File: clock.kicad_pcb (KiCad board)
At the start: 4 copper layers, 32 x 30 mm, 30 parts, among them J1 CONN_01X05, P1 USB_OTG, P2 CONN_01X02, U1 oled_i2c_display_128x64, U2 FM24V10-G, U3 STLCS01V1, U4 mcp73831, U5 lmv341, U6 NCP170

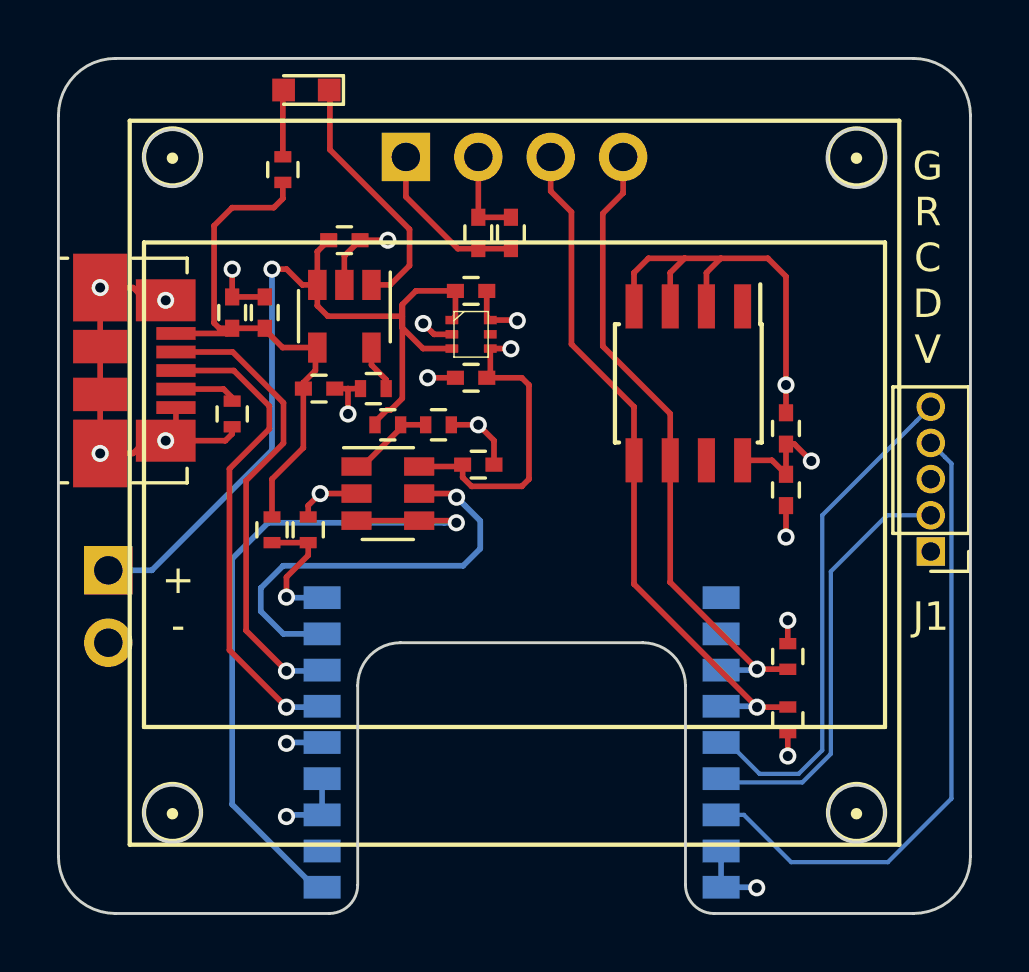
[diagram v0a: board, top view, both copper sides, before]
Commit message: modified ncp170 symbol because was totally wrong, F%*ç%
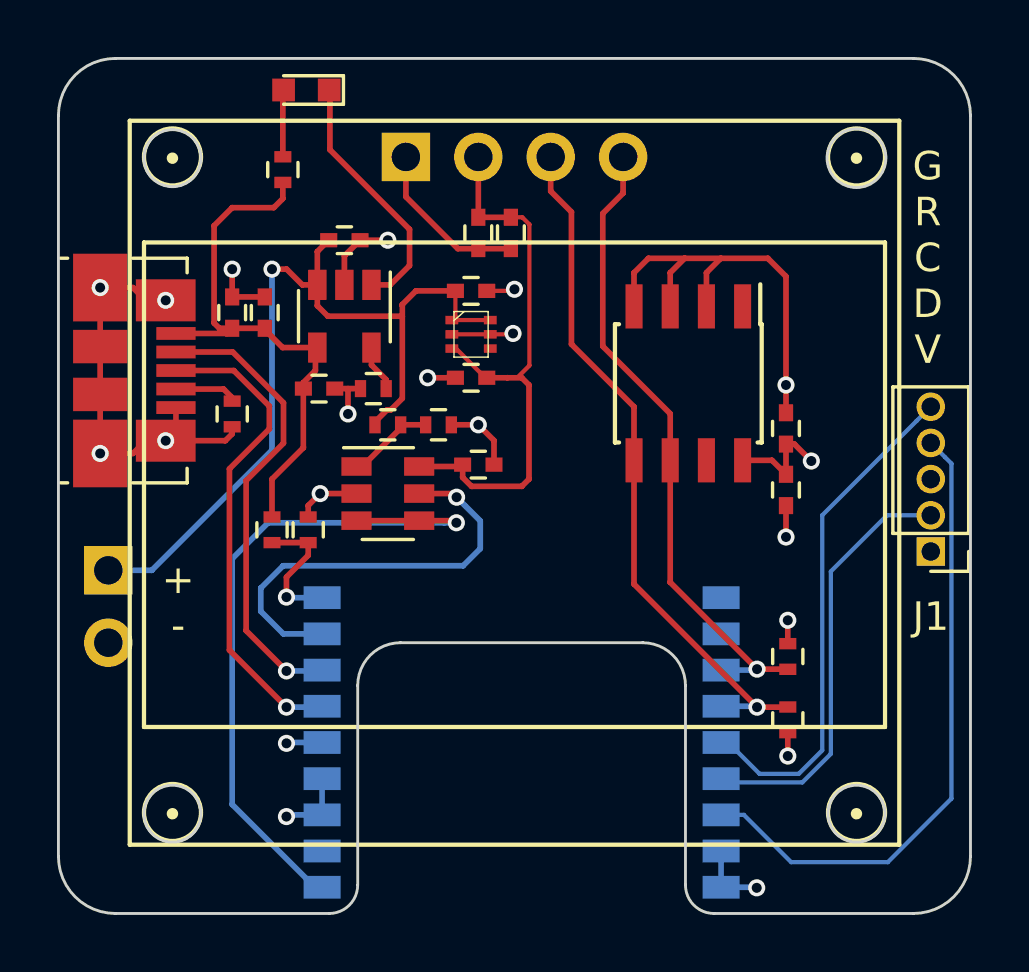
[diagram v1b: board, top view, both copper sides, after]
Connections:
- U6 pad 3: /VBAT -> VCC
- U6 pad 4: VCC -> (no net)
- U6 pad 5: (no net) -> GND
- U6 pad 6: GND -> /VBAT
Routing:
- net VCC: track 22.7 -> 29.4 mm, vias 5 -> 4
- net /VBAT: track 31.9 -> 30.5 mm
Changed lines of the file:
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@@
   (general
     (links 82)
-    (no_connects 0)
+    (no_connects 5)
     (area 149.949999 69.949999 182.050001 100.050001)
     (thickness 1.6)
     (drawings 30)
-    (tracks 264)
+    (tracks 265)
     (zones 0)
     (modules 30)
@@
       (net 1 GND))
     (pad 3 smd rect (at 0.5 0.675 270) (size 0.3 0.45) (layers F.Cu F.Paste F.Mask)
+      (net 2 VCC))
+    (pad 4 smd rect (at 0.5 -0.675 270) (size 0.3 0.45) (layers F.Cu F.Paste F.Mask))
+    (pad 5 smd rect (at 0 -0.675 270) (size 0.3 0.45) (layers F.Cu F.Paste F.Mask)
+      (net 1 GND))
+    (pad 6 smd rect (at -0.5 -0.675 270) (size 0.3 0.45) (layers F.Cu F.Paste F.Mask)
       (net 3 /VBAT))
-    (pad 4 smd rect (at 0.5 -0.675 270) (size 0.3 0.45) (layers F.Cu F.Paste F.Mask)
-      (net 2 VCC))
-    (pad 5 smd rect (at 0 -0.675 270) (size 0.3 0.45) (layers F.Cu F.Paste F.Mask))
-    (pad 6 smd rect (at -0.5 -0.675 270) (size 0.3 0.45) (layers F.Cu F.Paste F.Mask)
-      (net 1 GND))
   )
   (module Capacitors_SMD:C_0402 (layer F.Cu)
@@
   (gr_line (start 152 70) (end 180 70) (layer Edge.Cuts) (width 0.1))
   (gr_line (start 150 98) (end 150 72) (layer Edge.Cuts) (width 0.1))
+  (segment (start 165.92 79.68) (end 165.95 79.65) (width 0.15) (layer F.Cu) (net 1))
+  (segment (start 165.153 79.68) (end 165.92 79.68) (width 0.15) (layer F.Cu) (net 1))
+  (via (at 165.95 79.65) (size 0.6) (drill 0.35) (layers F.Cu B.Cu) (net 1))
+  (segment (start 165.028 78.156) (end 165.944 78.156) (width 0.15) (layer F.Cu) (net 1))
+  (via (at 166 78.1) (size 0.6) (drill 0.35) (layers F.Cu B.Cu) (net 1))
+  (segment (start 165.944 78.156) (end 166 78.1) (width 0.15) (layer F.Cu) (net 1))
+  (segment (start 163.803 79.68) (end 165.153 79.68) (width 0.15) (layer F.Cu) (net 1))
   (segment (start 174.48 99.08) (end 174.5 99.1) (width 0.2) (layer B.Cu) (net 1))
   (segment (start 173.25 99.08) (end 174.48 99.08) (width 0.2) (layer B.Cu) (net 1))
   (via (at 174.5 99.1) (size 0.6) (drill 0.35) (layers F.Cu B.Cu) (net 1))
-  (segment (start 166.08 79.18) (end 166.1 79.2) (width 0.2) (layer F.Cu) (net 1))
-  (segment (start 165.153 79.18) (end 166.08 79.18) (width 0.2) (layer F.Cu) (net 1))
-  (via (at 166.1 79.2) (size 0.6) (drill 0.35) (layers F.Cu B.Cu) (net 1))
-  (segment (start 163.180002 79.68) (end 163.100001 79.599999) (width 0.2) (layer F.Cu) (net 1))
-  (segment (start 163.100001 79.599999) (end 162.800002 79.3) (width 0.2) (layer F.Cu) (net 1))
-  (segment (start 163.803 79.68) (end 163.180002 79.68) (width 0.2) (layer F.Cu) (net 1))
-  (via (at 162.800002 79.3) (size 0.6) (drill 0.35) (layers F.Cu B.Cu) (net 1))
   (segment (start 164.732 76.674) (end 164.012 76.674) (width 0.2) (layer F.Cu) (net 1))
   (segment (start 164.012 76.674) (end 162.192 74.854) (width 0.2) (layer F.Cu) (net 1))
@@
   (segment (start 163.928 81.204) (end 162.954 81.204) (width 0.2) (layer F.Cu) (net 1) (status 10))
   (via (at 162.954 81.204) (size 0.6) (drill 0.35) (layers F.Cu B.Cu) (net 1))
-  (segment (start 165.028 78.156) (end 165.028 79.055) (width 0.2) (layer F.Cu) (net 1) (status 30))
-  (segment (start 165.028 79.055) (end 165.153 79.18) (width 0.2) (layer F.Cu) (net 1) (status 30))
   (segment (start 173.25 99.08) (end 173.25 97.81) (width 0.2) (layer B.Cu) (net 1) (status 30))
   (via (at 153.764 83.4125) (size 0.6) (drill 0.35) (layers F.Cu B.Cu) (net 1) (status 30))
@@
   (segment (start 152.614 78.04) (end 153.0615 78.4875) (width 0.2) (layer F.Cu) (net 1) (status 20))
   (segment (start 153.0615 78.4875) (end 153.764 78.4875) (width 0.2) (layer F.Cu) (net 1) (status 30))
+  (segment (start 166.256 81.204) (end 165.75 81.204) (width 0.2) (layer F.Cu) (net 2))
+  (segment (start 165.75 81.204) (end 165.028 81.204) (width 0.2) (layer F.Cu) (net 2))
+  (segment (start 166.525001 80.774999) (end 166.096 81.204) (width 0.15) (layer F.Cu) (net 2))
+  (segment (start 166.096 81.204) (end 165.75 81.204) (width 0.15) (layer F.Cu) (net 2))
+  (segment (start 165.875 75.574) (end 166.275 75.574) (width 0.15) (layer F.Cu) (net 2))
+  (segment (start 166.275 75.574) (end 166.525001 75.824001) (width 0.15) (layer F.Cu) (net 2))
+  (segment (start 166.525001 75.824001) (end 166.525001 80.774999) (width 0.15) (layer F.Cu) (net 2))
+  (segment (start 163.803 80.18) (end 163.954 80.18) (width 0.15) (layer F.Cu) (net 2))
+  (segment (start 163.954 80.18) (end 164.978 81.204) (width 0.15) (layer F.Cu) (net 2))
+  (segment (start 164.978 81.204) (end 165.028 81.204) (width 0.15) (layer F.Cu) (net 2))
   (segment (start 159.25 96.54) (end 158.06 96.54) (width 0.2) (layer B.Cu) (net 2))
   (segment (start 158.06 96.54) (end 158 96.6) (width 0.2) (layer B.Cu) (net 2))
@@
   (segment (start 164.732 73.457) (end 164.732 75.574) (width 0.2) (layer F.Cu) (net 2) (status 30))
   (segment (start 165.875 75.574) (end 164.732 75.574) (width 0.2) (layer F.Cu) (net 2) (status 30))
-  (segment (start 165.867 80.18) (end 165.875 80.188) (width 0.2) (layer F.Cu) (net 2))
-  (segment (start 165.153 80.18) (end 165.867 80.18) (width 0.2) (layer F.Cu) (net 2))
-  (via (at 165.875 80.188) (size 0.6) (drill 0.35) (layers F.Cu B.Cu) (net 2))
   (via (at 176.416 84.125) (size 0.6) (drill 0.35) (layers F.Cu B.Cu) (net 2))
   (segment (start 175.527 83.532) (end 175.527 84.591) (width 0.2) (layer F.Cu) (net 2) (status 30))
@@
   (segment (start 175.527 83.532) (end 175.527 83.582) (width 0.2) (layer F.Cu) (net 2) (status 30))
   (segment (start 166.51 81.458) (end 166.256 81.204) (width 0.2) (layer F.Cu) (net 2))
-  (segment (start 166.256 81.204) (end 165.028 81.204) (width 0.2) (layer F.Cu) (net 2) (status 20))
   (segment (start 166.51 84.76) (end 166.51 81.458) (width 0.2) (layer F.Cu) (net 2))
   (segment (start 166.256 85.014) (end 166.51 84.76) (width 0.2) (layer F.Cu) (net 2))
@@
   (segment (start 164.182 84.252) (end 164.182 84.702) (width 0.2) (layer F.Cu) (net 2) (status 10))
   (segment (start 164.182 84.702) (end 164.494 85.014) (width 0.2) (layer F.Cu) (net 2))
-  (segment (start 165.153 80.18) (end 165.153 81.079) (width 0.2) (layer F.Cu) (net 2) (status 30))
   (segment (start 165.153 81.079) (end 165.028 81.204) (width 0.2) (layer F.Cu) (net 2) (status 30))
   (segment (start 175.5905 93.6555) (end 175.5905 94.4755) (width 0.2) (layer F.Cu) (net 2) (status 10))
@@
   (segment (start 164.116 84.318) (end 164.182 84.252) (width 0.2) (layer F.Cu) (net 2) (status 30))
   (segment (start 159.25 96.54) (end 159.25 95.27) (width 0.2) (layer B.Cu) (net 2) (status 30))
+  (segment (start 162.05 78.65) (end 162.544 78.156) (width 0.2) (layer F.Cu) (net 3))
+  (segment (start 162.544 78.156) (end 163.928 78.156) (width 0.2) (layer F.Cu) (net 3))
+  (segment (start 163.803 79.18) (end 165.153 79.18) (width 0.15) (layer F.Cu) (net 3))
+  (segment (start 163.928 78.156) (end 163.928 79.055) (width 0.15) (layer F.Cu) (net 3))
+  (segment (start 163.928 79.055) (end 163.803 79.18) (width 0.15) (layer F.Cu) (net 3))
   (segment (start 159.083 77.945) (end 159.083 78.675) (width 0.2) (layer F.Cu) (net 3))
   (segment (start 159.083 78.675) (end 159.453 79.045) (width 0.2) (layer F.Cu) (net 3))
@@
   (segment (start 161.534001 82.327999) (end 161.664603 82.327999) (width 0.2) (layer F.Cu) (net 3))
   (segment (start 162.065 81.927602) (end 162.065 79.045) (width 0.2) (layer F.Cu) (net 3))
-  (segment (start 163.803 80.18) (end 162.792006 80.18) (width 0.2) (layer F.Cu) (net 3))
-  (segment (start 162.792006 80.18) (end 162.065 79.452994) (width 0.2) (layer F.Cu) (net 3))
-  (segment (start 162.065 79.452994) (end 162.065 78.664) (width 0.2) (layer F.Cu) (net 3))
   (segment (start 157.493 77.394) (end 157.493 83.744) (width 0.2) (layer B.Cu) (net 3))
   (segment (start 157.493 83.744) (end 153.277 87.96) (width 0.2) (layer B.Cu) (net 3))
   (segment (start 153.277 87.96) (end 151.75 87.96) (width 0.2) (layer B.Cu) (net 3))
   (segment (start 162.065 79.045) (end 162.065 78.635) (width 0.2) (layer F.Cu) (net 3))
-  (segment (start 162.065 78.635) (end 162.544 78.156) (width 0.2) (layer F.Cu) (net 3))
-  (segment (start 162.544 78.156) (end 163.928 78.156) (width 0.2) (layer F.Cu) (net 3) (status 20))
-  (segment (start 163.928 78.156) (end 163.928 79.055) (width 0.2) (layer F.Cu) (net 3) (status 30))
-  (segment (start 163.928 79.055) (end 163.803 79.18) (width 0.2) (layer F.Cu) (net 3) (status 30))
   (segment (start 158.007 77.394) (end 157.493 77.394) (width 0.2) (layer F.Cu) (net 3))
   (via (at 157.493 77.394) (size 0.6) (drill 0.35) (layers F.Cu B.Cu) (net 3))

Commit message: small modif
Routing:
- net GND: track 56.7 -> 58.1 mm
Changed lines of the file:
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@@
   (general
     (links 82)
-    (no_connects 5)
+    (no_connects 0)
     (area 149.949999 69.949999 182.050001 100.050001)
     (thickness 1.6)
     (drawings 30)
-    (tracks 265)
+    (tracks 266)
     (zones 0)
     (modules 30)
@@
   (gr_line (start 152 70) (end 180 70) (layer Edge.Cuts) (width 0.1))
   (gr_line (start 150 98) (end 150 72) (layer Edge.Cuts) (width 0.1))
+  (segment (start 165.95 78.15) (end 165.95 79.65) (width 0.15) (layer F.Cu) (net 1))
+  (segment (start 165.028 78.156) (end 165.944 78.156) (width 0.15) (layer F.Cu) (net 1))
+  (segment (start 165.944 78.156) (end 165.95 78.15) (width 0.15) (layer F.Cu) (net 1))
+  (via (at 165.95 78.15) (size 0.6) (drill 0.35) (layers F.Cu B.Cu) (net 1))
   (segment (start 165.92 79.68) (end 165.95 79.65) (width 0.15) (layer F.Cu) (net 1))
   (segment (start 165.153 79.68) (end 165.92 79.68) (width 0.15) (layer F.Cu) (net 1))
   (via (at 165.95 79.65) (size 0.6) (drill 0.35) (layers F.Cu B.Cu) (net 1))
-  (segment (start 165.028 78.156) (end 165.944 78.156) (width 0.15) (layer F.Cu) (net 1))
-  (via (at 166 78.1) (size 0.6) (drill 0.35) (layers F.Cu B.Cu) (net 1))
-  (segment (start 165.944 78.156) (end 166 78.1) (width 0.15) (layer F.Cu) (net 1))
   (segment (start 163.803 79.68) (end 165.153 79.68) (width 0.15) (layer F.Cu) (net 1))
   (segment (start 174.48 99.08) (end 174.5 99.1) (width 0.2) (layer B.Cu) (net 1))
